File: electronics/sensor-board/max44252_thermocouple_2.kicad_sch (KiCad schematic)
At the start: 21 parts

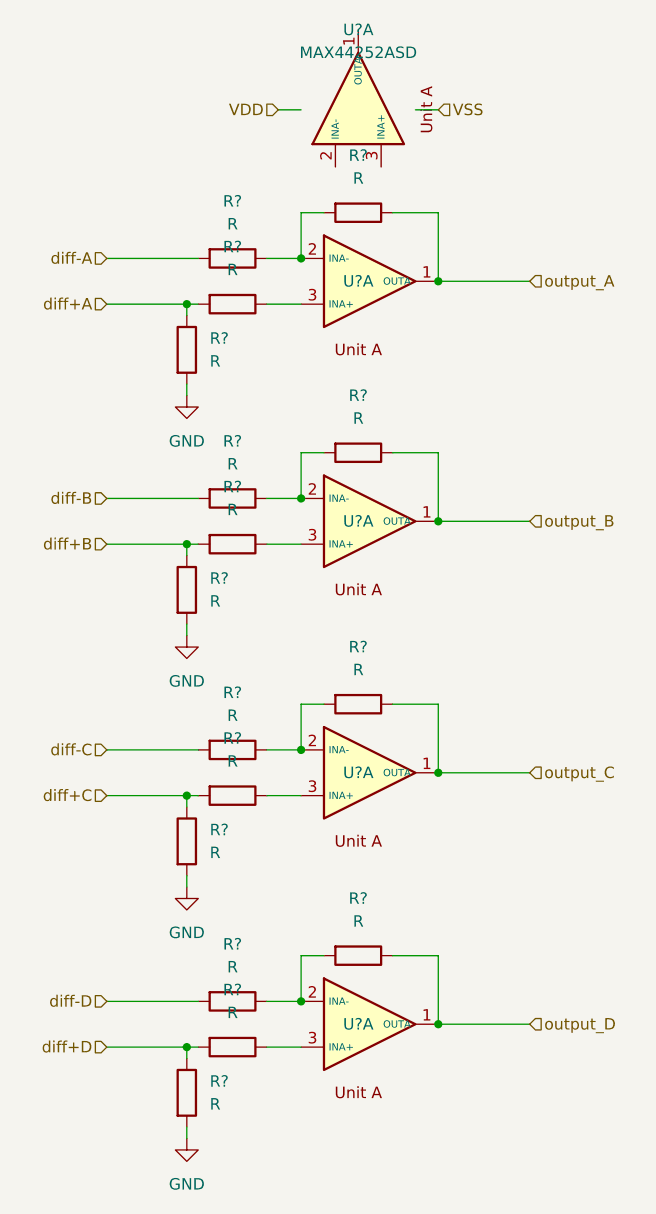
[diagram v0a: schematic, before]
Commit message: sensor-board edits
Finalized pressure and flow sensor circuits.
Reorganized schematics
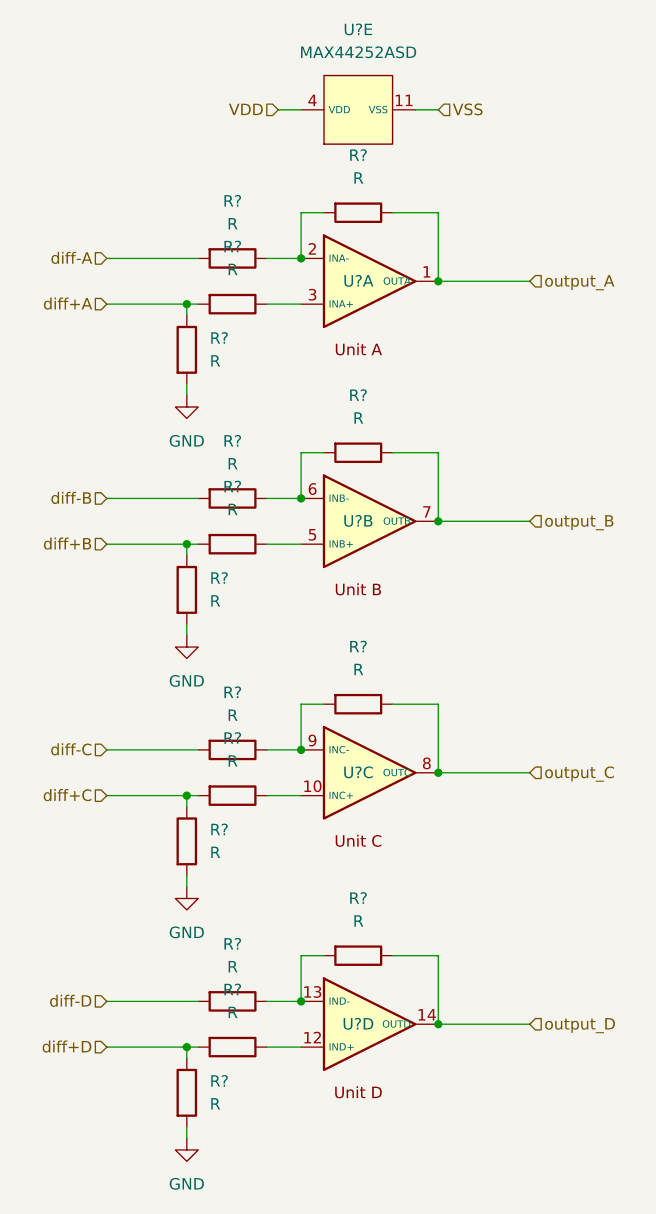
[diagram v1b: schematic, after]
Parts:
- removed R? (x2): R, symbol Device:R
- added R? (x2): R, symbol Device:R
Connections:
- net GND: now also R?.2
- net VDD: now also U?.4 (VDD)
- net VSS: now also U?.11 (VSS)
- net diff+A: now also R?.1, R?.2
- net output_B: now also U?.7 (OUTB); no longer U?.1 (OUTA)
- net output_C: now also U?.8 (OUTC); no longer U?.1 (OUTA)
- net output_D: now also U?.14 (OUTD); no longer U?.1 (OUTA)
- net at U?.3 (INA+): now also R?.1
- net at R?.1, R?.2: now also U?.9 (INC-); no longer U?.2 (INA-)
- net at R?.1: now also U?.10 (INC+); no longer U?.3 (INA+)
- net at R?.1, R?.2: now also U?.13 (IND-); no longer U?.2 (INA-)
- net at R?.1: now also U?.5 (INB+); no longer U?.3 (INA+)
- net at R?.1, R?.2: now also U?.6 (INB-); no longer U?.2 (INA-)
- net at R?.1: now also U?.12 (IND+); no longer U?.3 (INA+)
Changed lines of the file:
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@@
     (pin "2")
   )
-  (symbol (lib_id "MAX44252ASD_Custom:MAX44252ASD") (at 153.67 44.45 90) (unit 1)
+  (symbol (lib_id "MAX44252ASD_Custom:MAX44252ASD") (at 153.67 44.45 90) (unit 5)
     (in_bom yes) (on_board yes) (fields_autoplaced)
     (property "Reference" "U?" (id 0) (at 153.67 35.56 90))
@@
       (effects (font (size 1.27 1.27)) hide)
     )
-    (pin "1")
-    (pin "2")
-    (pin "3")
+    (pin "11")
+    (pin "4")
   )
   (symbol (lib_id "MAX44252ASD_Custom:MAX44252ASD") (at 153.67 63.5 0) (unit 1)
@@
     (pin "3")
   )
-  (symbol (lib_id "MAX44252ASD_Custom:MAX44252ASD") (at 153.67 90.17 0) (unit 1)
+  (symbol (lib_id "MAX44252ASD_Custom:MAX44252ASD") (at 153.67 90.17 0) (unit 2)
     (in_bom yes) (on_board yes)
     (property "Reference" "U?" (id 0) (at 153.67 90.17 0))
@@
       (effects (font (size 1.27 1.27)) hide)
     )
-    (pin "1")
-    (pin "2")
-    (pin "3")
+    (pin "5")
+    (pin "6")
+    (pin "7")
   )
-  (symbol (lib_id "MAX44252ASD_Custom:MAX44252ASD") (at 153.67 118.11 0) (unit 1)
+  (symbol (lib_id "MAX44252ASD_Custom:MAX44252ASD") (at 153.67 118.11 0) (unit 3)
     (in_bom yes) (on_board yes)
     (property "Reference" "U?" (id 0) (at 153.67 118.11 0))
@@
       (effects (font (size 1.27 1.27)) hide)
     )
-    (pin "1")
-    (pin "2")
-    (pin "3")
+    (pin "10")
+    (pin "8")
+    (pin "9")
   )
-  (symbol (lib_id "MAX44252ASD_Custom:MAX44252ASD") (at 153.67 146.05 0) (unit 1)
+  (symbol (lib_id "MAX44252ASD_Custom:MAX44252ASD") (at 153.67 146.05 0) (unit 4)
     (in_bom yes) (on_board yes)
     (property "Reference" "U?" (id 0) (at 153.67 146.05 0))
@@
       (effects (font (size 1.27 1.27)) hide)
     )
-    (pin "1")
-    (pin "2")
-    (pin "3")
+    (pin "12")
+    (pin "13")
+    (pin "14")
   )
   (sheet_instances
